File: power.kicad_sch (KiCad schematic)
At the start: 19 parts, among them J9 DC Barrel Jack, U2 LMR33630B, U3 TLV76733

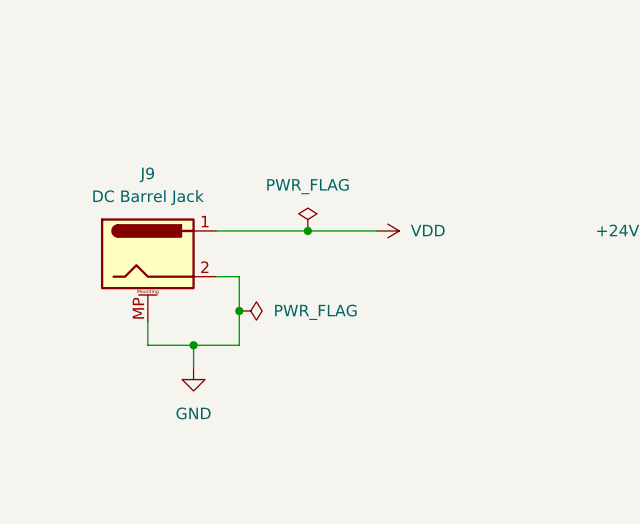
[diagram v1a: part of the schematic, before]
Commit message: Updated power connector
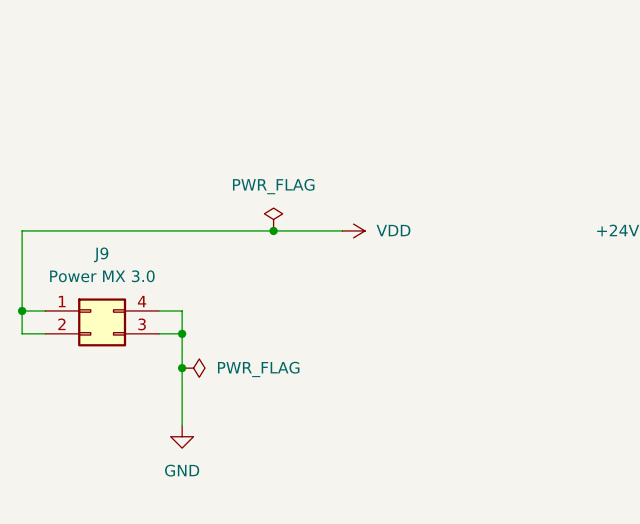
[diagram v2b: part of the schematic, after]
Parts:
- removed J9: DC Barrel Jack, Connector_BarrelJack:BarrelJack_Horizontal, symbol Connector:Barrel_Jack_MountingPin
- added J9: Power MX 3.0, Connector_Molex:Molex_Micro-Fit_3.0_43045-0400_2x02_P3.00mm_Horizontal, symbol Connector_Generic:Conn_02x02_Counter_Clockwise
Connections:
- net GND: now also J9.3 (Pin_3), J9.4 (Pin_4)
- net VDD: now also J9.1 (Pin_1), J9.2 (Pin_2)
